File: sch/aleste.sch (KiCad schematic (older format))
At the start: 11 parts, among them P1 PIN, P2 PIN, P3 PIN, P4 PIN, P5 PIN, P6 PIN, X1 SLOT-62

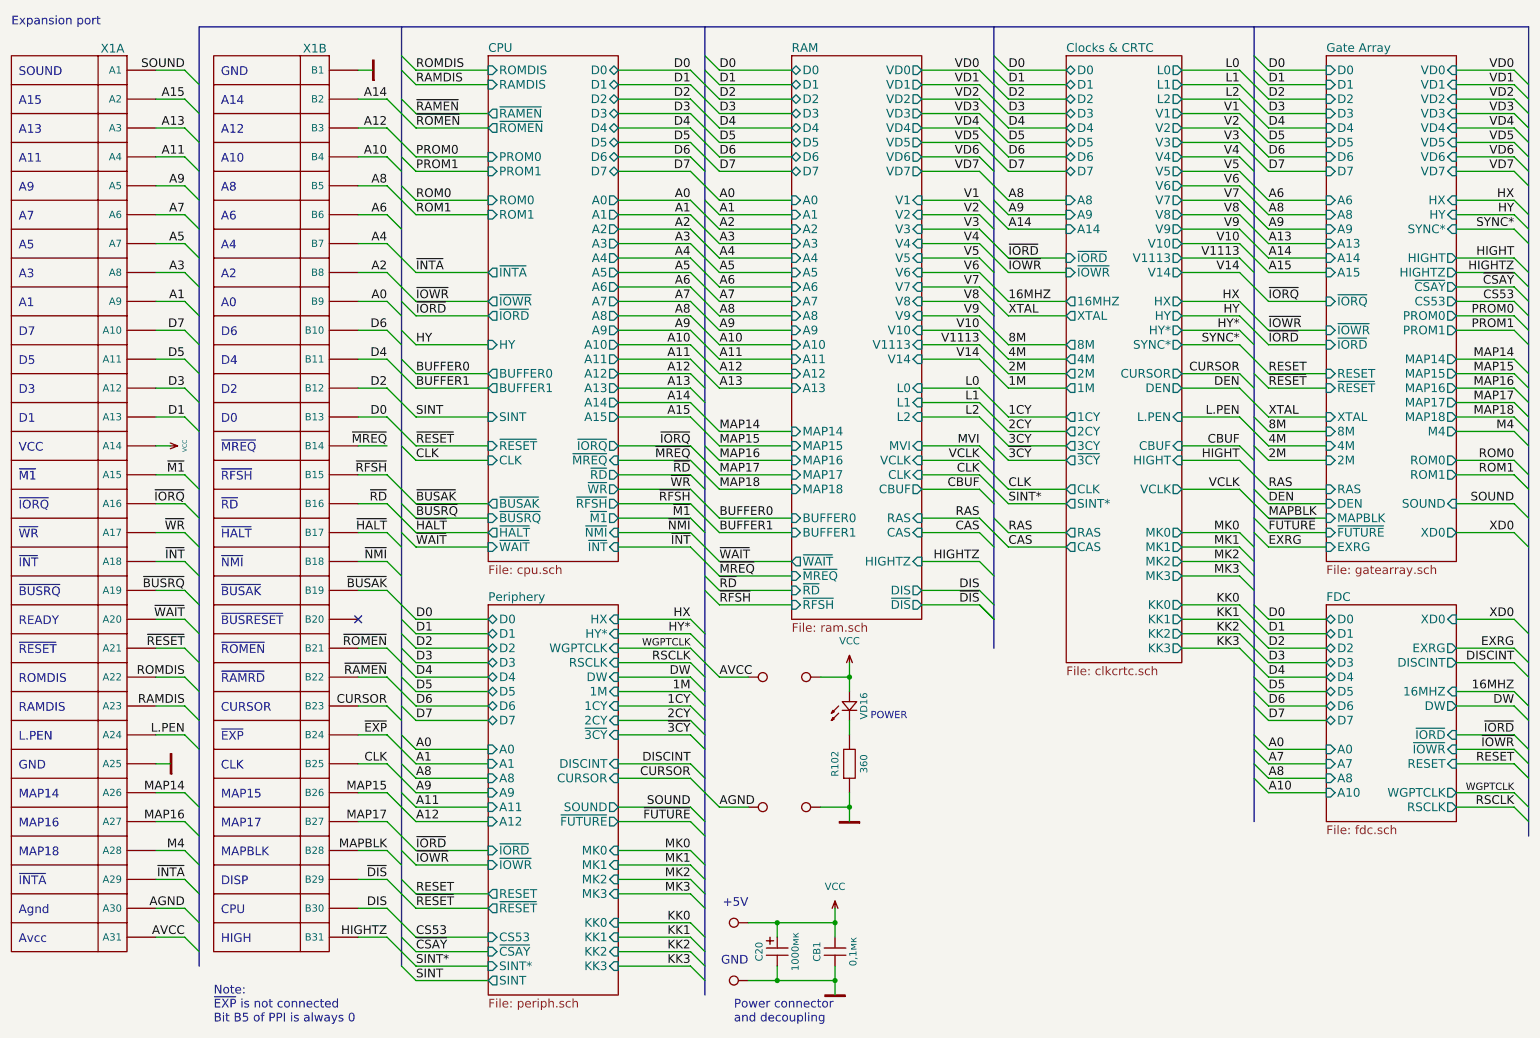
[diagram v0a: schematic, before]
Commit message: Start to move to a bit more affordable components
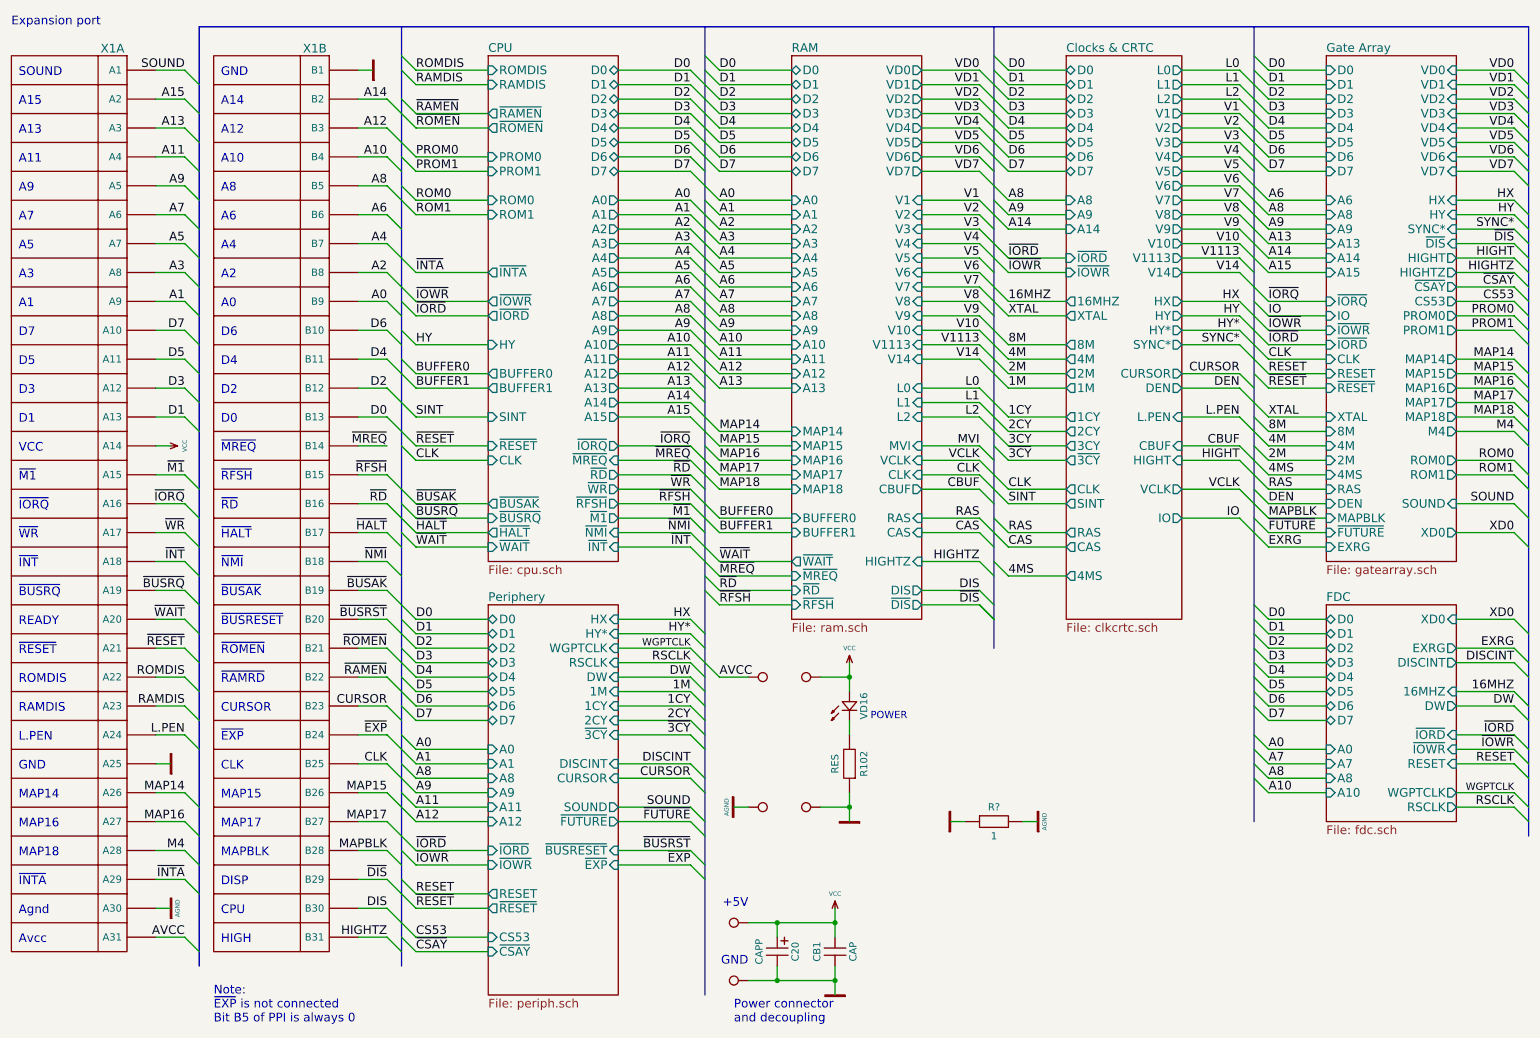
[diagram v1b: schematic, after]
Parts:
- added R?: 1, symbol RES
- C20: value 1000мк -> CAPP
- CB1: value 0,1мк -> CAP
- R102: value 360 -> RES
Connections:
- net AGND is gone; now on net GND: P4.1, X1.A30
- net GND: now also R?.1, R?.2
- net ~BUSRST: now reaches X1.B20
- no-connect marks 1 -> 0

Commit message: Fix MVI signal
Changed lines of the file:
@@
 F59 "IO" I L 9700 2700 60
 F60 "CLK" I L 9700 3000 60
+F61 "MVI" O R 10600 4300 60
 $EndSheet
 $Sheet
@@
 Wire Wire Line
 	1700 6800 1600 6800
+Wire Wire Line
+	10600 4300 11000 4300
+Entry Wire Line
+	11000 4300 11100 4400
+Text Label 11000 4300 2    60   ~ 0
+MVI
 $EndSCHEMATC
